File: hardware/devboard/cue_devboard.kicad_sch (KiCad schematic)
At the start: 57 parts, among them J1 USB-C (power), J2 BATT, J3 LRA, J4 SWD, J5 EXP, SW1 USER, SW2 SHIP/WAKE, U1 BL54L15u, U2 nPM1300, U3 LSM6DSV16BX, U4 T5838, U5 DRV2605L

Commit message: Dev board: real BL54L15u footprint, routed 38x28 layout, JLCPCB fab package
- BL54L15u 453-00223 footprint from the Ezurio datasheet land pattern (p.25);
  module edge-centred with >=15 mm board edge each side, 3x5 mm antenna
  keep-out on all layers. Board grows to 38 x 28 mm.
- Placement reworked around the nPM1300 with reserved escape lanes; grid
  router (maze_patch.py) finishes what Freerouting leaves open.
- DRC: 0 violations, 0 unconnected. PCB pad nets match the circuit (56/56).
- Dropped the optional P1.12 spare (R9, J5 pin 10): Note 7 says leave unused.
- fab/: Gerbers + drill zip, JLCPCB BOM with LCSC numbers, CPL, assembly and
  schematic PDFs. Board, project and fab files now tracked in git.

Co-Authored-By: Claude Opus 5.5 <noreply@anthropic.com>
Claude-Session: https://claude.ai/code/session_01DUSU7jbUyc6QVB5XjyAbxC
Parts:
- removed R9: 330R, Resistor_SMD:R_0402_1005Metric, symbol Device:R
- RT1: Note 10k 1% B25/50 3380 K (nPM1300 PS Table 11). Place next to J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 -> 10k 1% B25/50 3380 K (nPM1300 PS Table 11). Next to U2: wit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
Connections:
- net EXP_P1_12: no longer names the net of J5.10 (NC)
- net U1_EXP_P1_12: no longer names the net of U1.19 (P1.12)
- no-connect marks 31 -> 33
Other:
- note added: "Ezurio Note 7: P1.09-P1.12 toggle below 1 MHz behind >=330 R (R7-R8); no I2C or fast clocks there."
- note removed: "Ezurio Note 7: P1.09-P1.12 toggle below 1 MHz behind >=330 R (R7-R9); no I2C or fast clocks there."
- moved on the sheet: C16, J4, R7, R8, SW1, U1

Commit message: Dev board: regulator layout per Nordic guide; full footprint review
Independent footprint/pin-map review against manufacturer drawings for all
parts found no errors. Layout review against nPM1300 PS 9.3.4 / Fig. 62-65:
- SW1/SW2: hand-routed 2.5 mm, 0.3 mm wide, no vias (was 6-9 mm at 0.127 mm
  through 2 vias each); L1/L2 2.3 mm from the pins, output caps at the
  inductor outputs, PVDD cap 1.5 mm from pin 4.
- Exposed pad: 3x3 GND vias (was 2x2), matching Nordic's reference.
- Power tracks widened after routing where clearance allows (0.2-0.4 mm).
- Escape lane for the LSM6DSV16BX 1V8 pin; cleanup loop routes anything a
  stub removal leaves open. DRC: 0 errors, 0 unconnected.
- J2/U5 footprints re-homed in Cue.pretty with project-local 3D models.
- README: review results, firmware requirements, optional rev B items.

Co-Authored-By: Claude Opus 5.5 <noreply@anthropic.com>
Claude-Session: https://claude.ai/code/session_01DUSU7jbUyc6QVB5XjyAbxC
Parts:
- J2: footprint Connector_JST:JST_PH_S2B-PH-SM4-TB_1x02-1MP_P2.00mm_Horizontal -> Cue:JST_PH_S2B-PH-SM4-TB_1x02-1MP_P2.00mm_Horizontal
- U4: Note SELECT=GND -> right channel. Bottom port: 0.8 mm board hole. -> SELECT=GND -> right channel (data after the falling clock e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
- U5: footprint Package_SO:VSSOP-10_3x3mm_P0.5mm -> Cue:VSSOP-10_3x3mm_P0.5mm
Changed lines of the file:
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@@
     (property "Reference" "J2" (at 91.44 99.06 0) (effects (font (size 1.27 1.27))))
     (property "Value" "BATT" (at 91.44 114.3 0) (effects (font (size 1.27 1.27))))
-    (property "Footprint" "Connector_JST:JST_PH_S2B-PH-SM4-TB_1x02-1MP_P2.00mm_Horizontal" (at 91.44 106.68 0) (effects (font (size 1.27 1.27)) hide))
+    (property "Footprint" "Cue:JST_PH_S2B-PH-SM4-TB_1x02-1MP_P2.00mm_Horizontal" (at 91.44 106.68 0) (effects (font (size 1.27 1.27)) hide))
     (property "Datasheet" "" (at 91.44 106.68 0) (effects (font (size 1.27 1.27)) hide))
     (property "MPN" "JST S2B-PH-SM4-TB" (at 91.44 106.68 0) (effects (font (size 1.27 1.27)) hide))
@@
     (property "Reference" "U5" (at 180.34 166.37 0) (effects (font (size 1.27 1.27))))
     (property "Value" "DRV2605L" (at 180.34 189.23 0) (effects (font (size 1.27 1.27))))
-    (property "Footprint" "Package_SO:VSSOP-10_3x3mm_P0.5mm" (at 180.34 177.8 0) (effects (font (size 1.27 1.27)) hide))
+    (property "Footprint" "Cue:VSSOP-10_3x3mm_P0.5mm" (at 180.34 177.8 0) (effects (font (size 1.27 1.27)) hide))
     (property "Datasheet" "" (at 180.34 177.8 0) (effects (font (size 1.27 1.27)) hide))
     (property "MPN" "TI DRV2605LDGSR" (at 180.34 177.8 0) (effects (font (size 1.27 1.27)) hide))
@@
     (property "Datasheet" "" (at 312.42 55.88 0) (effects (font (size 1.27 1.27)) hide))
     (property "MPN" "TDK InvenSense T5838" (at 312.42 55.88 0) (effects (font (size 1.27 1.27)) hide))
-    (property "Note" "SELECT=GND -> right channel. Bottom port: 0.8 mm board hole." (at 312.42 55.88 0) (effects (font (size 1.27 1.27)) hide))
+    (property "Note" "SELECT=GND -> right channel (data after the falling clock edge). Bottom port: 0.6 mm board hole (TDK: 0.5-1.0)." (at 312.42 55.88 0) (effects (font (size 1.27 1.27)) hide))
     (pin "7")
     (pin "6")

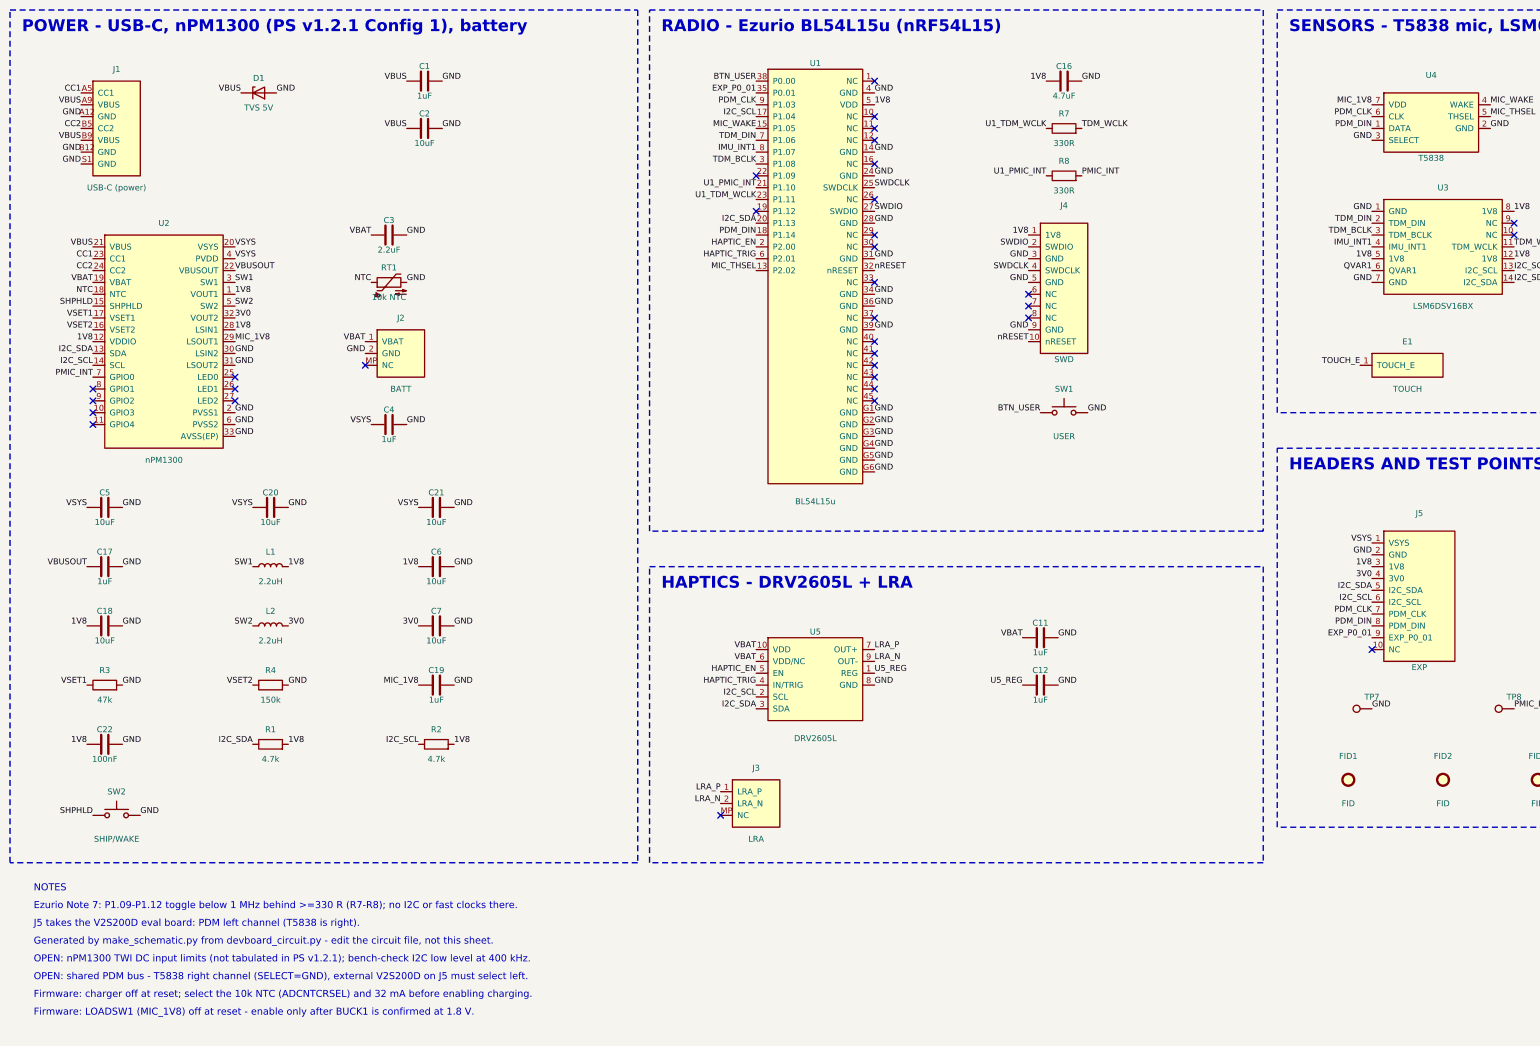
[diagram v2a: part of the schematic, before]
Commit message: Dev board: switch radio to Ezurio BL54L15 453-00044 (in stock), 42 x 32 mm
The BL54L15u (453-00223) is out of stock until ~Dec 2026. The dev board now uses
the larger BL54L15 with an MHF4 antenna connector:
- new 39-pad footprint from the Ezurio BL54L10/BL54L15 land pattern, 3D model
- same nRF54L15 port pins as the cuff (firmware unchanged), new pad numbers
- board 42 x 32 mm, re-placed and re-routed: DRC 0 violations, 0 unconnected,
  board = circuit pad for pad
- BOM: U1 453-00044C (global sourcing), J1 -> C5246813 (USB4125-GF-A-0190)
- READMEs: antenna to buy, ordering notes

Co-Authored-By: Claude Opus 5.5 <noreply@anthropic.com>
Claude-Session: https://claude.ai/code/session_01DUSU7jbUyc6QVB5XjyAbxC
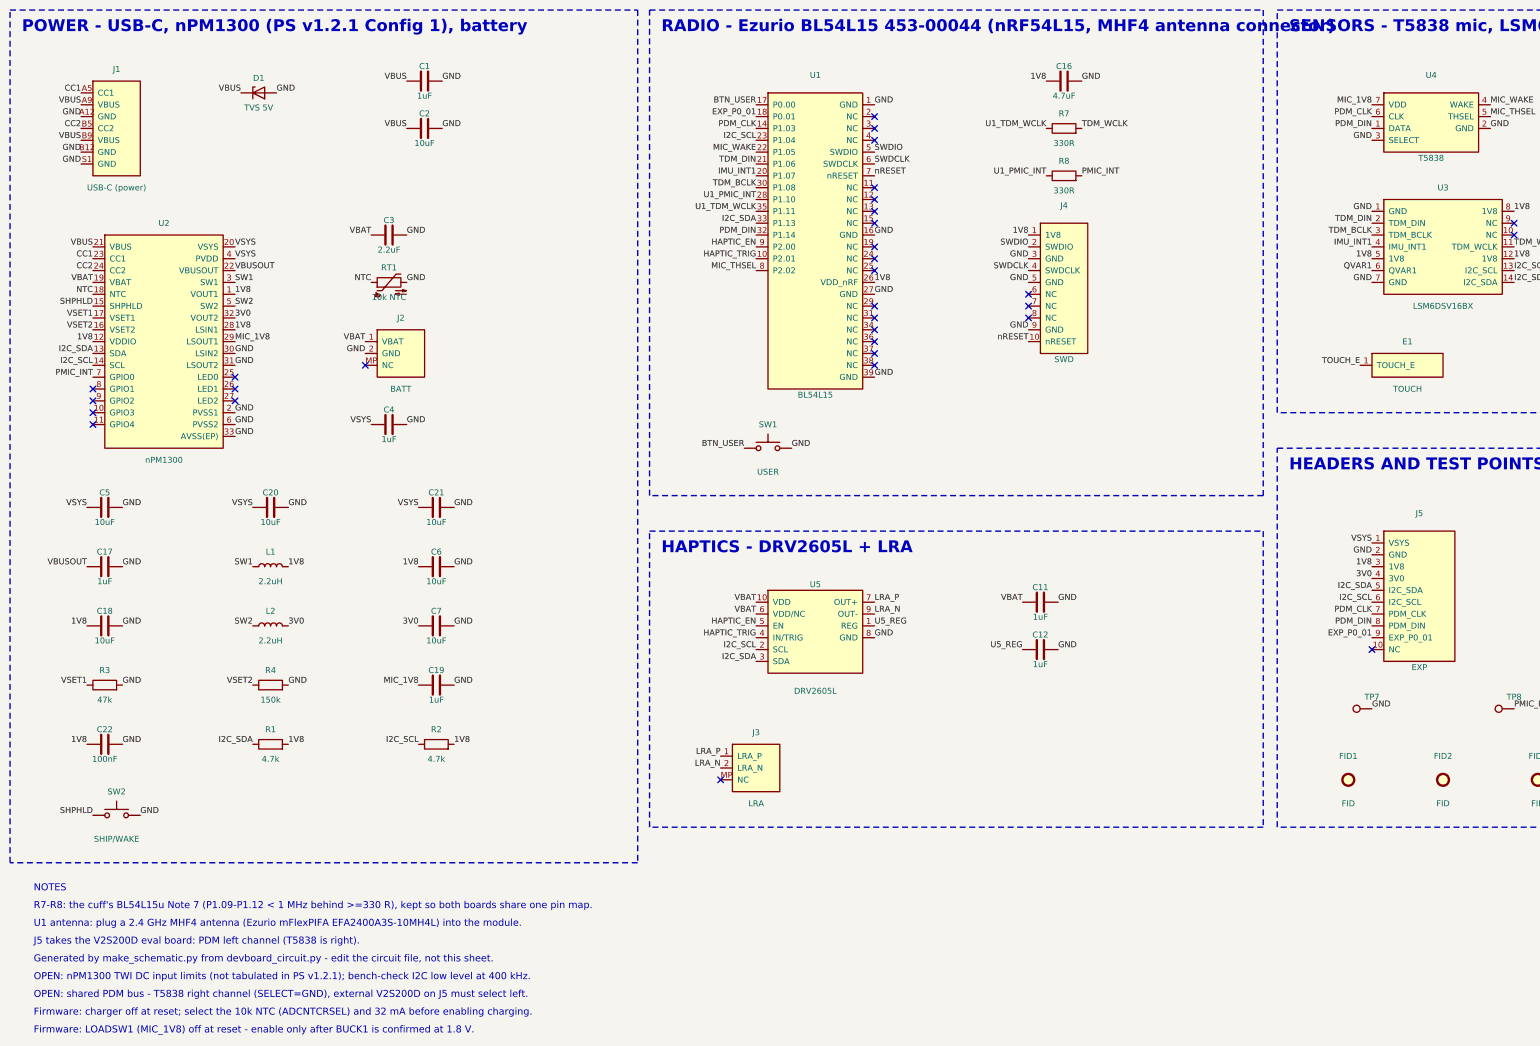
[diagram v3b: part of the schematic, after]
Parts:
- R7, R8: Note Ezurio Note 7: >=330 R series on P1.09-P1.12; place at U1 p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 -> Cuff (BL54L15u) Ezurio Note 7: >=330 R series on P1.09-P1.1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
- U1: value BL54L15u -> BL54L15; footprint Cue:Ezurio_BL54L15u_453-00223 -> Cue:Ezurio_BL54L15_453-00044; MPN Ezurio 453-00223 -> Ezurio 453-00044; Note Certified nRF54L15 module, chip antenna, 7.9x6.3x1.75 mm. P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 -> Certified nRF54L15 module, 14x10x1.6 mm, MHF4 connector for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
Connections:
- net 1V8: now also U1.26 (VDD_nRF); no longer U1.5 (VDD)
- net BTN_USER: now also U1.17 (P0.00); no longer U1.38 (P0.00)
- net EXP_P0_01: now also U1.18 (P0.01); no longer U1.35 (P0.01)
- net GND: now also U1.1 (GND), U1.16 (GND), U1.27 (GND); no longer U1.14 (GND), U1.24 (GND), U1.28 (GND), U1.31 (GND), U1.34 (GND), U1.36 (GND), U1.4 (GND), U1.G1 (GND), U1.G2 (GND), U1.G3 (GND), U1.G4 (GND), U1.G5 (GND), U1.G6 (GND)
- net HAPTIC_EN: now also U1.9 (P2.00); no longer U1.2 (P2.00)
- net HAPTIC_TRIG: now also U1.10 (P2.01); no longer U1.6 (P2.01)
- net I2C_SCL: now also U1.23 (P1.04); no longer U1.17 (P1.04)
- net I2C_SDA: now also U1.33 (P1.13); no longer U1.20 (P1.13)
- net IMU_INT1: now also U1.20 (P1.07); no longer U1.8 (P1.07)
- net MIC_THSEL: now also U1.8 (P2.02); no longer U1.13 (P2.02)
- net MIC_WAKE: now also U1.22 (P1.05); no longer U1.15 (P1.05)
- net PDM_CLK: now also U1.14 (P1.03); no longer U1.9 (P1.03)
- net PDM_DIN: now also U1.32 (P1.14); no longer U1.18 (P1.14)
- net SWDCLK: now also U1.6 (SWDCLK); no longer U1.25 (SWDCLK)
- net SWDIO: now also U1.5 (SWDIO); no longer U1.27 (SWDIO)
- net TDM_BCLK: now also U1.30 (P1.08); no longer U1.3 (P1.08)
- net TDM_DIN: now also U1.21 (P1.06); no longer U1.7 (P1.06)
- net U1_PMIC_INT: now also U1.28 (P1.10); no longer U1.21 (P1.10)
- net U1_TDM_WCLK: now also U1.35 (P1.11); no longer U1.23 (P1.11)
- net nRESET: now also U1.7 (nRESET); no longer U1.32 (nRESET)
- no-connect marks 33 -> 31
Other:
- note added: "R7-R8: the cuff's BL54L15u Note 7 (P1.09-P1.12 < 1 MHz behind >=330 R), kept so both boards share one pin map."
- note added: "RADIO - Ezurio BL54L15 453-00044 (nRF54L15, MHF4 antenna connector)"
- note added: "U1 antenna: plug a 2.4 GHz MHF4 antenna (Ezurio mFlexPIFA EFA2400A3S-10MH4L) into the module."
- note removed: "Ezurio Note 7: P1.09-P1.12 toggle below 1 MHz behind >=330 R (R7-R8); no I2C or fast clocks there."
- note removed: "RADIO - Ezurio BL54L15u (nRF54L15)"
- moved on the sheet: C11, C12, J3, SW1, U5

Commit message: Dev board: fixes from the second layout review
- battery polarity marked (+/-) at J2; README: meter the cell's plug first
- LRA connector moved so the motor lines stay 2 mm from PDM_CLK, 5 mm from the mic hole
- nPM1300 exposed pad: 4 vias in the gaps between paste openings (no solder wicking)
- vias moved off the RT1, C6, C8 pads (via_off_pads.py); L1 joins C6 on top copper
- U3 pin 7 tied to ground (C8 shifted 0.4 mm, QVAR1 re-routed)
- silkscreen at JLCPCB minimums (1.0 mm text), TP net labels, button labels on top
- SW1/SW2 left out of BOM/CPL (hand-solder); fab/placement_check.png for the JLCPCB preview
DRC 0 violations, 0 unconnected; board = circuit pad for pad.

Co-Authored-By: Claude Opus 5.5 <noreply@anthropic.com>
Claude-Session: https://claude.ai/code/session_01DUSU7jbUyc6QVB5XjyAbxC
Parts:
- J2: Note JST-PH to fit the Adafruit #1570 100 mAh LiPo (built-in pro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 -> JST-PH for the Adafruit #1570 LiPo. Pin 1 = + (silk '+'). J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
- SW1: Note (none) -> Hand-solder: out of stock at LCSC.
- SW2: Note Hold to leave ship mode / power on. -> Hold to leave ship mode / power on. Hand-solder: out of sto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
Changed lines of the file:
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@@
     (property "Datasheet" "" (at 91.44 106.68 0) (effects (font (size 1.27 1.27)) hide))
     (property "MPN" "JST S2B-PH-SM4-TB" (at 91.44 106.68 0) (effects (font (size 1.27 1.27)) hide))
-    (property "Note" "JST-PH to fit the Adafruit #1570 100 mAh LiPo (built-in protection). Check polarity: pin 1 = +." (at 91.44 106.68 0) (effects (font (size 1.27 1.27)) hide))
+    (property "Note" "JST-PH for the Adafruit #1570 LiPo. Pin 1 = + (silk '+'). JST-PH battery leads are not standardised: meter the cell's plug before connecting; red must land on '+'." (at 91.44 106.68 0) (effects (font (size 1.27 1.27)) hide))
     (pin "1")
     (pin "2")
@@
     (property "Datasheet" "" (at 30.48 205.74 0) (effects (font (size 1.27 1.27)) hide))
     (property "MPN" "Omron B3U-1000P" (at 30.48 205.74 0) (effects (font (size 1.27 1.27)) hide))
-    (property "Note" "Hold to leave ship mode / power on." (at 30.48 205.74 0) (effects (font (size 1.27 1.27)) hide))
+    (property "Note" "Hold to leave ship mode / power on. Hand-solder: out of stock at LCSC." (at 30.48 205.74 0) (effects (font (size 1.27 1.27)) hide))
     (pin "1")
     (pin "2")
@@
     (property "Datasheet" "" (at 170.18 127 0) (effects (font (size 1.27 1.27)) hide))
     (property "MPN" "Omron B3U-1000P" (at 170.18 127 0) (effects (font (size 1.27 1.27)) hide))
-    (pin "1")
-    (pin "2")
+    (property "Note" "Hand-solder: out of stock at LCSC." (at 170.18 127 0) (effects (font (size 1.27 1.27)) hide))
+    (pin "1")
+    (pin "2")

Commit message: Schematic: add MFG, MFG P/N, DIST, DIST P/N fields to every bought part
Values come from devboard_circuit.SOURCING (LCSC numbers already checked by
the JLCPCB BOM match). U1 is distributed by Newark since LCSC doesn't stock it.
Test points, fiducials and the touch pad are copper only and get no fields.

Co-Authored-By: Claude Opus 5.5 <noreply@anthropic.com>
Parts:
- C1, C11, C12, C17, C19, C4: DIST (none) -> LCSC; DIST P/N (none) -> C52923; MFG (none) -> Samsung Electro-Mechanics; MFG P/N (none) -> CL05A105KA5NQNC
- C10, C22, C8, C9: DIST (none) -> LCSC; DIST P/N (none) -> C1525; MFG (none) -> Samsung Electro-Mechanics; MFG P/N (none) -> CL05B104KO5NNNC
- C16: DIST (none) -> LCSC; DIST P/N (none) -> C23733; MFG (none) -> Samsung Electro-Mechanics; MFG P/N (none) -> CL05A475MP5NRNC
- C18, C2, C20, C21, C5, C6, C7: DIST (none) -> LCSC; DIST P/N (none) -> C96446; MFG (none) -> Samsung Electro-Mechanics; MFG P/N (none) -> CL10A106MA8NRNC
- C3: DIST (none) -> LCSC; DIST P/N (none) -> C23630; MFG (none) -> Samsung Electro-Mechanics; MFG P/N (none) -> CL10A225KO8NNNC
- D1: DIST (none) -> LCSC; DIST P/N (none) -> C82044; MFG (none) -> onsemi; MFG P/N (none) -> ESD5Z5.0T1G
- J1: DIST (none) -> LCSC; DIST P/N (none) -> C5246813; MFG (none) -> GCT; MFG P/N (none) -> USB4125-GF-A-0190
- J2: DIST (none) -> LCSC; DIST P/N (none) -> C295747; MFG (none) -> JST; MFG P/N (none) -> S2B-PH-SM4-TB(LF)(SN)
- J3: DIST (none) -> LCSC; DIST P/N (none) -> C160402; MFG (none) -> JST; MFG P/N (none) -> SM02B-SRSS-TB(LF)(SN)
- J4: DIST (none) -> LCSC; DIST P/N (none) -> C2932107; MFG (none) -> Samtec; MFG P/N (none) -> FTSH-105-01-L-DV-K-P-TR
- J5: DIST (none) -> LCSC; DIST P/N (none) -> C492422; MFG (none) -> XFCN; MFG P/N (none) -> PZ254V-12-10P
- L1, L2: DIST (none) -> LCSC; DIST P/N (none) -> C2049745; MFG (none) -> Murata Electronics; MFG P/N (none) -> DFE201210U-2R2M=P2
- R1, R2: DIST (none) -> LCSC; DIST P/N (none) -> C25900; MFG (none) -> UNI-ROYAL (Uniroyal Elec); MFG P/N (none) -> 0402WGF4701TCE
- R3: DIST (none) -> LCSC; DIST P/N (none) -> C25792; MFG (none) -> UNI-ROYAL (Uniroyal Elec); MFG P/N (none) -> 0402WGF4702TCE
- R4: DIST (none) -> LCSC; DIST P/N (none) -> C25755; MFG (none) -> UNI-ROYAL (Uniroyal Elec); MFG P/N (none) -> 0402WGF1503TCE
- R6: DIST (none) -> LCSC; DIST P/N (none) -> C17168; MFG (none) -> UNI-ROYAL (Uniroyal Elec); MFG P/N (none) -> 0402WGF0000TCE
- R7, R8: DIST (none) -> LCSC; DIST P/N (none) -> C25104; MFG (none) -> UNI-ROYAL (Uniroyal Elec); MFG P/N (none) -> 0402WGF3300TCE
- RT1: DIST (none) -> LCSC; DIST P/N (none) -> C77131; MFG (none) -> Murata Electronics; MFG P/N (none) -> NCP15XH103F03RC
- SW1, SW2: DIST (none) -> LCSC; DIST P/N (none) -> C231329; MFG (none) -> Omron; MFG P/N (none) -> B3U-1000P
- U1: DIST (none) -> Newark; MFG (none) -> Ezurio; MFG P/N (none) -> 453-00044C
- U2: DIST (none) -> LCSC; DIST P/N (none) -> C7466043; MFG (none) -> Nordic Semiconductor; MFG P/N (none) -> NPM1300-QEAA-R
- U3: DIST (none) -> LCSC; DIST P/N (none) -> C5267394; MFG (none) -> STMicroelectronics; MFG P/N (none) -> LSM6DSV16BXTR
- U4: DIST (none) -> LCSC; DIST P/N (none) -> C7230692; MFG (none) -> TDK InvenSense; MFG P/N (none) -> MMICT5838-00-012
- U5: DIST (none) -> LCSC; DIST P/N (none) -> C527464; MFG (none) -> Texas Instruments; MFG P/N (none) -> DRV2605LDGSR

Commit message: Schematic: wire the power block like the nPM1300 reference; GND symbols
The power block (nPM1300, USB-C, battery, bucks, load switches) is now drawn
with wires laid out like nPM1300 PS Figure 2. Only nets that continue into
other blocks keep a label (VBUS, VBAT, VSYS, 1V8, 3V0, MIC_1V8, I2C, PMIC_INT).
Ground is the power:GND symbol everywhere, with a PWR_FLAG for ERC. Sheet is A2.

check_schematic.py reads KiCad 8+ netlists and matches wire-only nets by pads;
make_schematic.py takes KICAD7_SYMBOL_DIR. Netlist check: 56 parts, 41 nets,
0 problems.

Co-Authored-By: Claude Opus 5.5 <noreply@anthropic.com>
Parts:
- U1: Note Certified nRF54L15 module, 14x10x1.6 mm, MHF4 connector for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 -> Hand-solder (castellated pads). Certified nRF54L15 module, 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
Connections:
- net CC1: no longer names the net of J1.A5 (CC1), U2.23 (CC1)
- net CC2: no longer names the net of J1.B5 (CC2), U2.24 (CC2)
- net NTC: no longer names the net of RT1.1, U2.18 (NTC)
- net SHPHLD: no longer names the net of SW2.1, U2.15 (SHPHLD)
- net SW1: no longer names the net of L1.1, U2.3 (SW1)
- net SW2: no longer names the net of L2.1, U2.5 (SW2)
- net VBUSOUT: no longer names the net of C17.1, U2.22 (VBUSOUT)
- net VSET1: no longer names the net of R3.1, U2.17 (VSET1)
- net VSET2: no longer names the net of R4.1, U2.16 (VSET2)
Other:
- moved on the sheet: C1, C10, C11, C12, C16, C17, C18, C19, C2, C20, C21, C22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
